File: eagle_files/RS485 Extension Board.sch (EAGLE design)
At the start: 4 parts, among them J1 RJ12 - 1, J2 RJ12 - 2, J3 RJ12 - 3, J4 RJ12 - 4

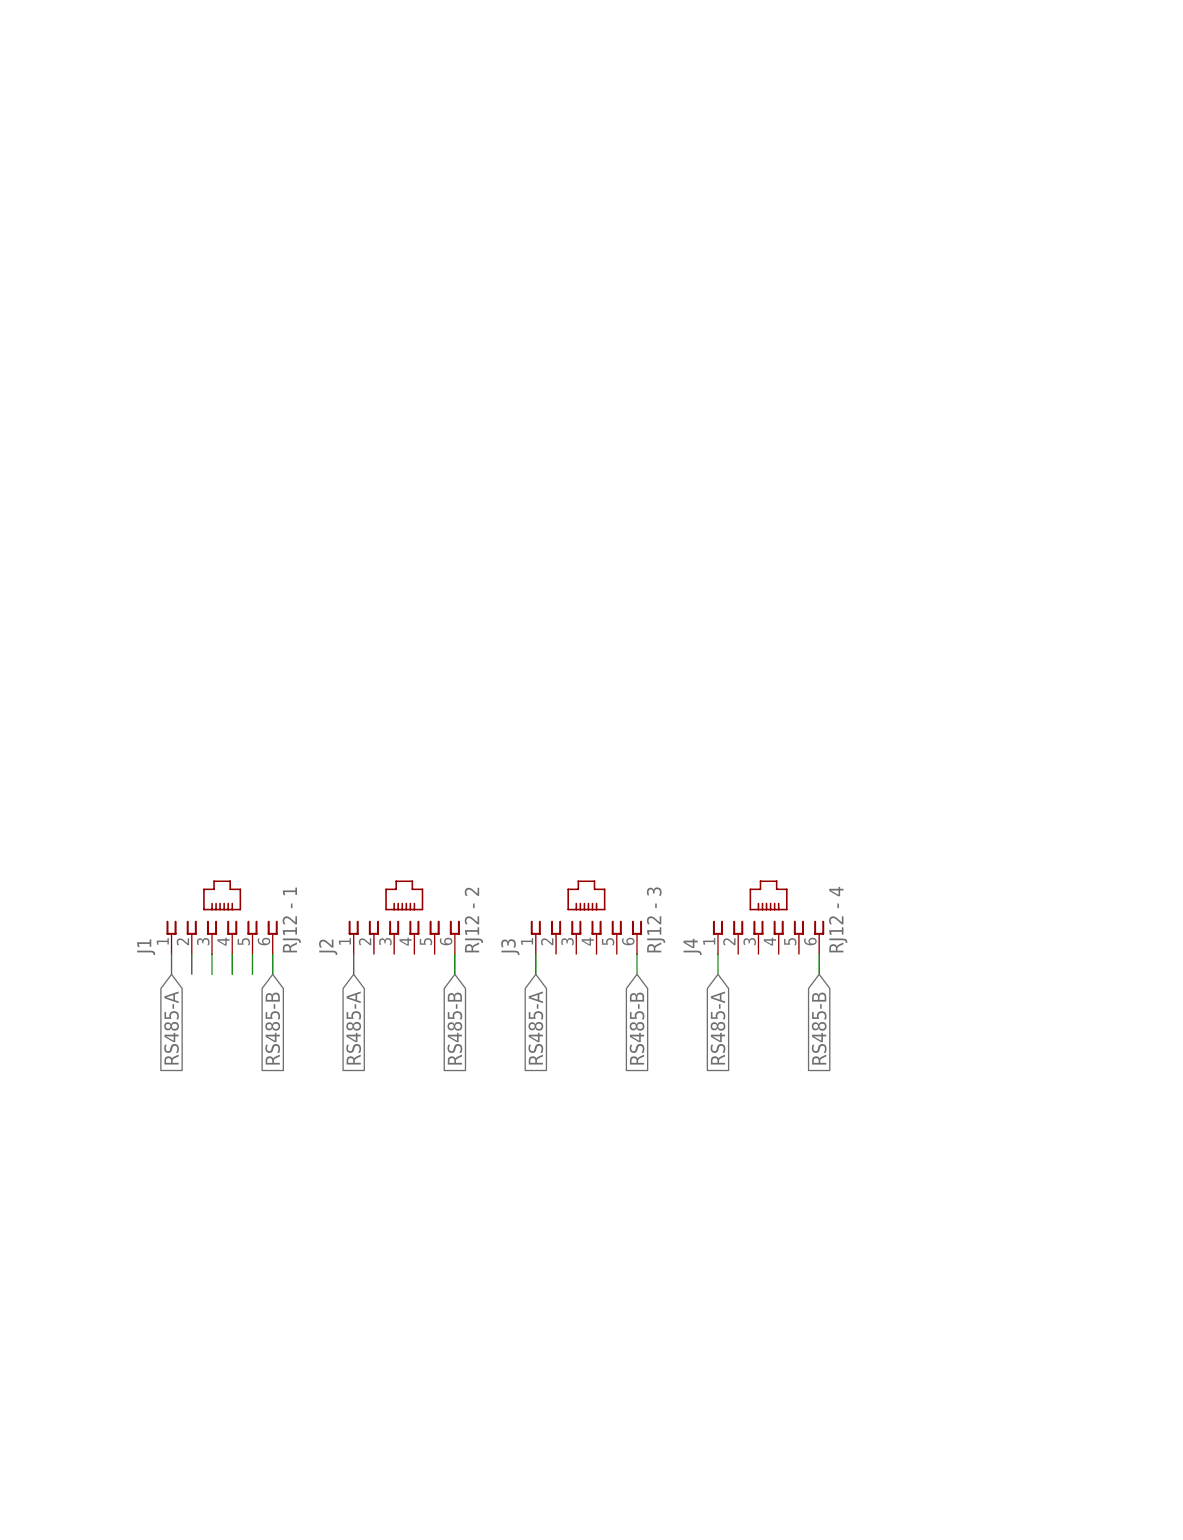
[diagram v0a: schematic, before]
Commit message: add connector and ic
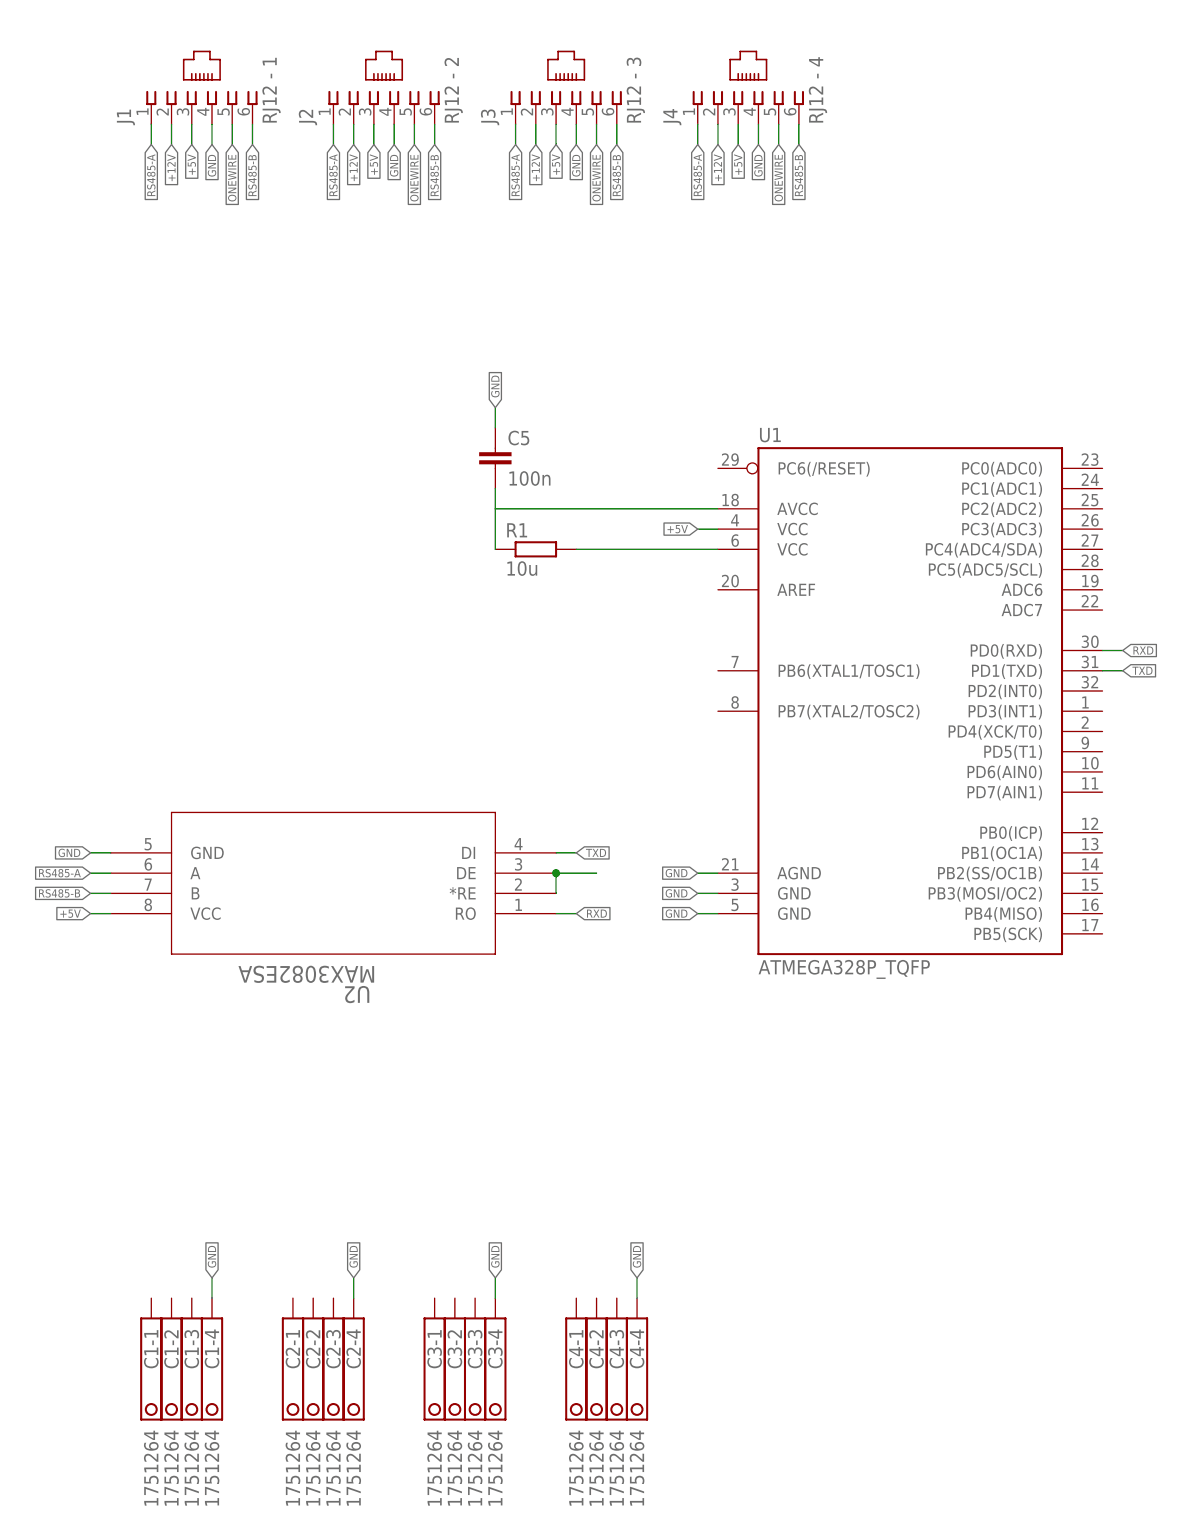
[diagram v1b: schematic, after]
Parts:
- added C1, C2, C3, C4: 1751264, con-phoenix-350:1751264
- added C5: 100n, rcl:C-EUC0805
- added R1: 10u, rcl:R-EU_M0805
- added U1: ATMEGA328P_TQFP, SparkFun-DigitalIC:ATMEGA328P_TQFP
- added U2: MAX3082ESA, MAX3082ESA:MAX3082ESA
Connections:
- removed net N$3: J1.4
- removed net N$4: J1.5
- new net +12V: J1.2, J2.2, J3.2, J4.2
- new net +5V: C5.2, J1.3, J2.3, J3.3, J4.3, R1.1, U1.AVCC, U1.VCC@4, U2.VCC
- new net GND: C1-4.K, C2-4.K, C3-4.K, C4-4.K, C5.1, J1.4, J2.4, J3.4, J4.4, U1.AGND, U1.GND@3, U1.GND@5, U2.GND
- new net ONEWIRE: J1.5, J2.5, J3.5, J4.5
- new net RXD: U1.PD0(RXD), U2.RO
- new net TXD: U1.PD1(TXD), U2.DI
- net N$1: now also U2.*RE, U2.DE; no longer J1.2
- net N$2: now also R1.2, U1.VCC@6; no longer J1.3
- net RS485-A: now also U2.A
- net RS485-B: now also U2.B
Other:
- moved on the sheet: J1, J2, J3, J4
